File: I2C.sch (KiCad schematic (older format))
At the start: 6 parts, among them Q1 BSS138, Q2 BSS138

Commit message: Added RS refs
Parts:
- Q1, Q2: RS (none) -> 545-2529
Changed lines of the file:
@@
 F 2 "Package_TO_SOT_SMD:SOT-23_Handsoldering" H 3050 3225 50  0001 L CIN
 F 3 "https://www.fairchildsemi.com/datasheets/BS/BSS138.pdf" H 2850 3300 50  0001 L CNN
+F 4 "545-2529" H 0   0   50  0001 C CNN "RS"
 	1    2850 3300
 	0    -1   -1   0
@@
 F 2 "Package_TO_SOT_SMD:SOT-23_Handsoldering" H 3600 3625 50  0001 L CIN
 F 3 "https://www.fairchildsemi.com/datasheets/BS/BSS138.pdf" H 3400 3700 50  0001 L CNN
+F 4 "545-2529" H 0   0   50  0001 C CNN "RS"
 	1    3400 3700
 	0    -1   -1   0

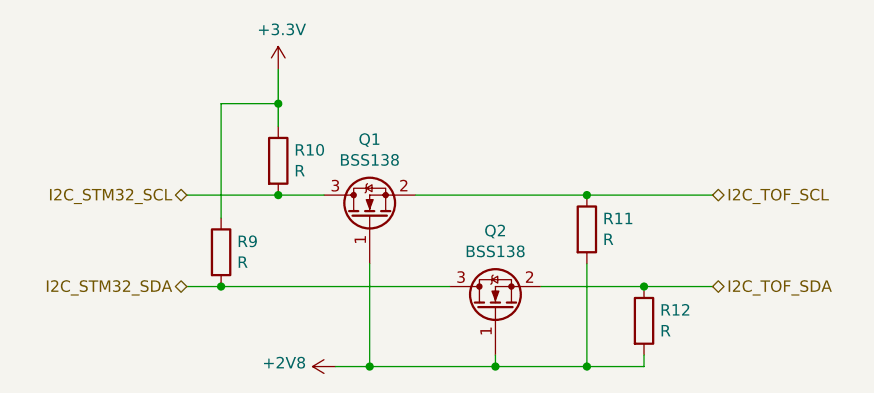
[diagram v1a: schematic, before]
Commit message: Added resistors values
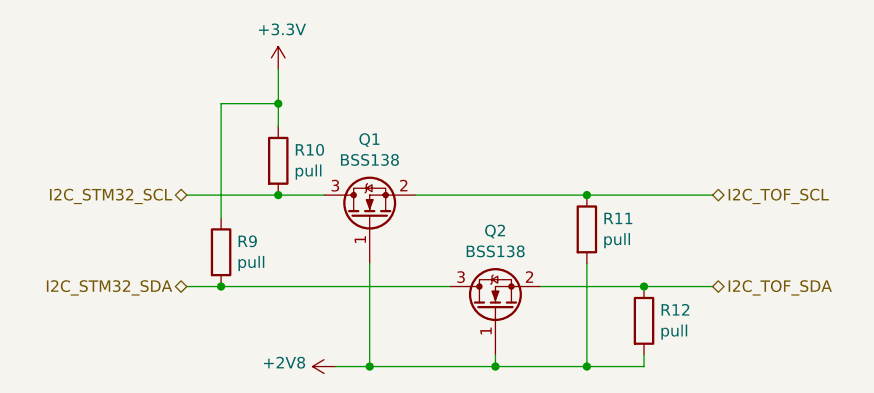
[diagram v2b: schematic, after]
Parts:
- R10, R11, R12, R9: value R -> pull
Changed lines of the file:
@@
 P 2200 3450
 F 0 "R9" H 2270 3496 50  0000 L CNN
-F 1 "R" H 2270 3405 50  0000 L CNN
+F 1 "pull" H 2270 3405 50  0000 L CNN
 F 2 "Resistor_SMD:R_0805_2012Metric_Pad1.15x1.40mm_HandSolder" V 2130 3450 50  0001 C CNN
 F 3 "~" H 2200 3450 50  0001 C CNN
@@
 P 2450 3050
 F 0 "R10" H 2520 3096 50  0000 L CNN
-F 1 "R" H 2520 3005 50  0000 L CNN
+F 1 "pull" H 2520 3005 50  0000 L CNN
 F 2 "Resistor_SMD:R_0805_2012Metric_Pad1.15x1.40mm_HandSolder" V 2380 3050 50  0001 C CNN
 F 3 "~" H 2450 3050 50  0001 C CNN
@@
 P 3800 3350
 F 0 "R11" H 3870 3396 50  0000 L CNN
-F 1 "R" H 3870 3305 50  0000 L CNN
+F 1 "pull" H 3870 3305 50  0000 L CNN
 F 2 "Resistor_SMD:R_0805_2012Metric_Pad1.15x1.40mm_HandSolder" V 3730 3350 50  0001 C CNN
 F 3 "~" H 3800 3350 50  0001 C CNN
@@
 P 4050 3750
 F 0 "R12" H 4120 3796 50  0000 L CNN
-F 1 "R" H 4120 3705 50  0000 L CNN
+F 1 "pull" H 4120 3705 50  0000 L CNN
 F 2 "Resistor_SMD:R_0805_2012Metric_Pad1.15x1.40mm_HandSolder" V 3980 3750 50  0001 C CNN
 F 3 "~" H 4050 3750 50  0001 C CNN
